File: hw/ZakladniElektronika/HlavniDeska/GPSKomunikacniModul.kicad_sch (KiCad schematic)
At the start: 5 parts, among them J3 Conn_2Rows-75Pins

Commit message: Nastin schematu
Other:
- moved on the sheet: D125, J3, R5, R8, U53

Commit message: Zavazbení zapínání
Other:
- note added: "W_DISABLE"
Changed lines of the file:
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@@
     (stroke (width 0.25) (type default) (color 0 0 0 1))
+  )
+  (text "W_DISABLE" (at 149.86 118.11 0)
+    (effects (font (size 1.27 1.27)) (justify left bottom))
   )
   (label "SIM_CD" (at 151.13 157.48 0) (fields_autoplaced)
@@
         )
         (path "/99cd3e15-4eb6-4cbb-8726-789aedd3df15/c3b70d9b-0dcb-4344-9507-13ff5b4c000e/2d5c8383-b4dd-4e50-a76e-5d9de1ae531a"
-          (reference "LED") (unit 1)
-        )
-      )
+          (reference "LED6") (unit 1)
+        )
+      )

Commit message: USB_multiplexer a přehlednost
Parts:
- added R13: 200k, Resistor_SMD:R_0402_1005Metric, symbol Device:R
- added R14, R16: 0-nc, symbol Device:R
- added R15, R17: 0, Resistor_SMD:R_0805_2012Metric_Pad1.20x1.40mm_HandSolder, symbol Device:R
- added U5: PCA9306DC, Package_SO:VSSOP-8_2.3x2mm_P0.5mm, symbol Interface:PCA9306DC
- added U6, U8: TXB0304RUT, Package_DFN_QFN:Texas_R-PUQFN-N12, symbol Logic_LevelTranslator:TXB0304RUT
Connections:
- net 1V8: now also U5.2 (VREF1), U6.1 (VCCA), U8.1 (VCCA)
- net 3V3: now also R13.1, U6.11 (VCCB)
- net CTS: now also U6.8 (B3)
- net DTR: now also U8.9 (B2)
- net GND: now also U5.1 (GND), U6.6 (GND), U8.6 (GND)
- net RST: now also U8.10 (B1)
- net RTS: now also U6.7 (B4)
- net RXD: now also U6.9 (B2)
- net SCL: now also U5.6 (SCL2)
- net SCL(1.8V): now also U5.3 (SCL1)
- net SDA: now also U5.5 (SDA2)
- net SDA(1.8V): now also U5.4 (SDA1)
- net TXD: now also U6.10 (B1)
- net UART_CTS(O)(1.8V): now also U6.4 (A3)
- net UART_DTR(I)(1.8V): now also U8.3 (A2)
- net UART_RTS(I)(1.8V): now also U6.5 (A4)
- net UART_RXD(I)(1.8V): now also R14.1, R15.1, U6.3 (A2); no longer J3.58 (Pin_58)
- net UART_TXD(O)(1.8V): now also R16.1, R17.1, U6.2 (A1); no longer J3.60 (Pin_60)
- net at J3.62 (Pin_62): now also R15.2
- net at J3.64 (Pin_64): now also R17.2
- net PNU0/LVD: no longer names the net of J3.67 (Pin_67)
- net PNU0/LVD: now also U8.2 (A1)
- net USB_D+ renamed D-
- net USB_D- renamed D+
- net WoWWAN(INT) renamed INT
- new net: R13.2, U5.7 (VREF2), U5.8 (EN)
- new net: J3.60 (Pin_60), R16.2
- new net: J3.58 (Pin_58), R14.2
- no-connect marks 37 -> 35
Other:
- removed sheet PNU0
- removed sheet PNU1
- removed sheet PNU2
- removed sheet PNU3
- removed sheet PNU4
- removed sheet PNU5
- removed sheet PNU6
- removed sheet PNU7
- moved on the sheet: D125, R5, U53

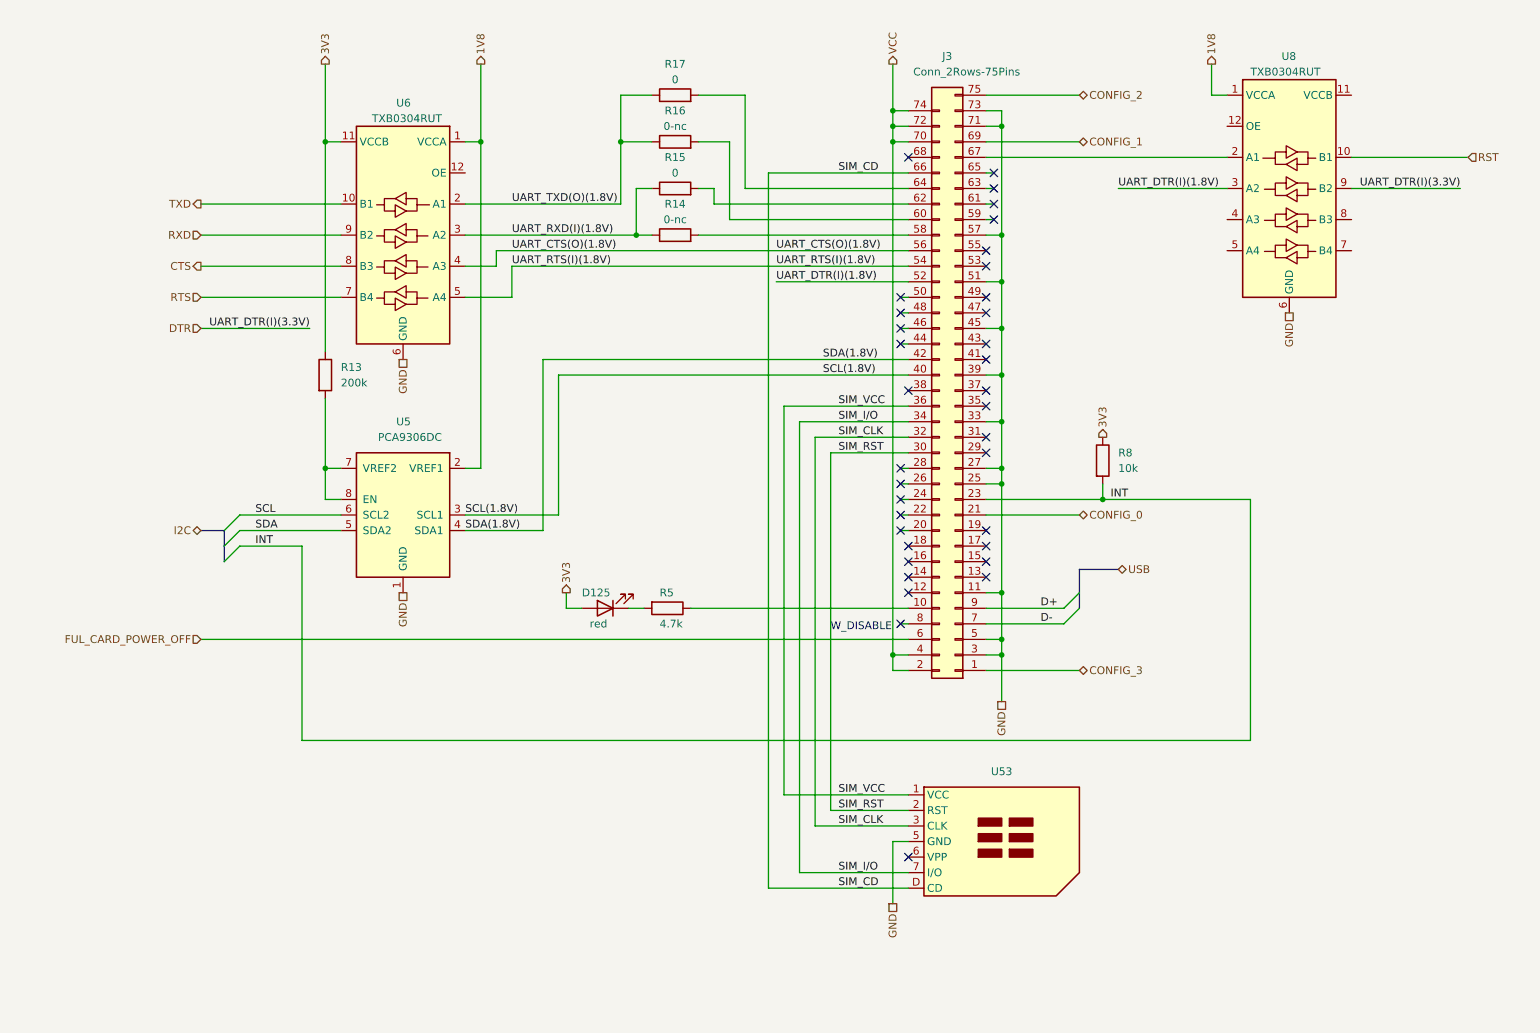
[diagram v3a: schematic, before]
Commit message: Likvidace MiniUI jako samostatné desky a výběr všech komponent
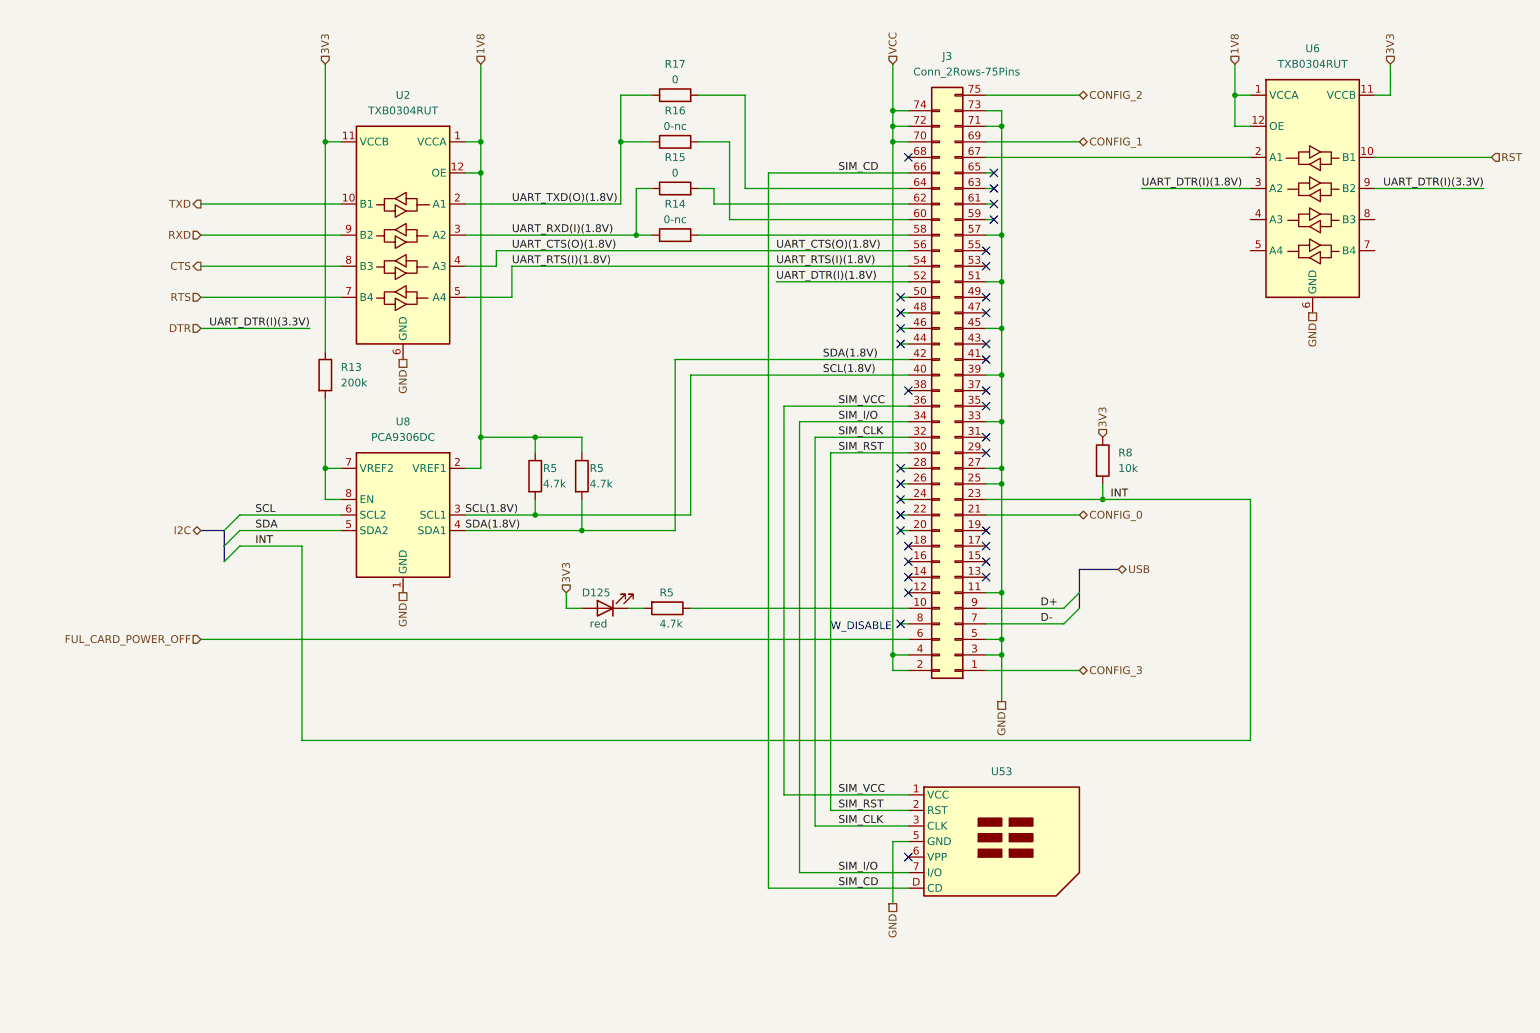
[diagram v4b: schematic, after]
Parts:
- removed U5: PCA9306DC, Package_SO:VSSOP-8_2.3x2mm_P0.5mm, symbol Interface:PCA9306DC
- removed U6, U8: TXB0304RUT, Package_DFN_QFN:Texas_R-PUQFN-N12, symbol Logic_LevelTranslator:TXB0304RUT
- added R5 (x2): 4.7k, Resistor_SMD:R_0402_1005Metric, symbol Device:R
- added U2, U6: TXB0304RUT, Package_DFN_QFN:Texas_R-PUQFN-N12, symbol RKL-BusCnverters:TXB0304RUT
- added U8: PCA9306DC, Package_SO:VSSOP-8_2.3x2mm_P0.5mm, symbol RKL-BusCnverters:PCA9306DC
- J3: footprint Robotarna_KiCad_Library:Conn_M2 -> RKL-Connectors:Conn_M2; Basic/Extended (none) -> E
- R14, R16: footprint (none) -> Resistor_SMD:R_0805_2012Metric_Pad1.20x1.40mm_HandSolder; JLCPCB_IGNORE (none) -> ignore
- R15, R17: Basic/Extended (none) -> B; LCSC C908865 -> C17477
- R5: footprint Resistor_SMD:R_0201_0603Metric -> Resistor_SMD:R_0402_1005Metric; Basic/Extended E -> B; LCSC C270346 -> C25900
- R8: Basic/Extended (none) -> B
- U53: footprint (none) -> RKL-Connectors:SMN-305-ARP7; Basic/Extended (none) -> E; LCSC (none) -> C720512
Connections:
- net 1V8: now also R5.1, R5.1, U2.1 (VCCA), U2.12 (OE), U6.1 (VCCA), U6.12 (OE), U8.2 (VREF1)
- net 3V3: now also U2.11 (VCCB), U6.11 (VCCB)
- net CTS: now also U2.8 (B3)
- net DTR: now also U6.9 (B2)
- net GND: now also U2.6 (GND), U6.6 (GND), U8.1 (GND)
- net RST: now also U6.10 (B1)
- net RTS: now also U2.7 (B4)
- net RXD: now also U2.9 (B2)
- net SCL: now also U8.6 (SCL2)
- net SCL(1.8V): now also R5.2, U8.3 (SCL1)
- net SDA: now also U8.5 (SDA2)
- net SDA(1.8V): now also R5.2, U8.4 (SDA1)
- net TXD: now also U2.10 (B1)
- net UART_CTS(O)(1.8V): now also U2.4 (A3)
- net UART_DTR(I)(1.8V): now also U6.3 (A2)
- net UART_RTS(I)(1.8V): now also U2.5 (A4)
- net UART_RXD(I)(1.8V): now also U2.3 (A2)
- net UART_TXD(O)(1.8V): now also U2.2 (A1)
- net at R13.2: now also U8.7 (VREF2), U8.8 (EN)
- net at J3.67 (Pin_67): now also U6.2 (A1)

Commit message: Výmněna ochrany baterie
Předchozí ochranný čip JLCPCB nemělo na skladě
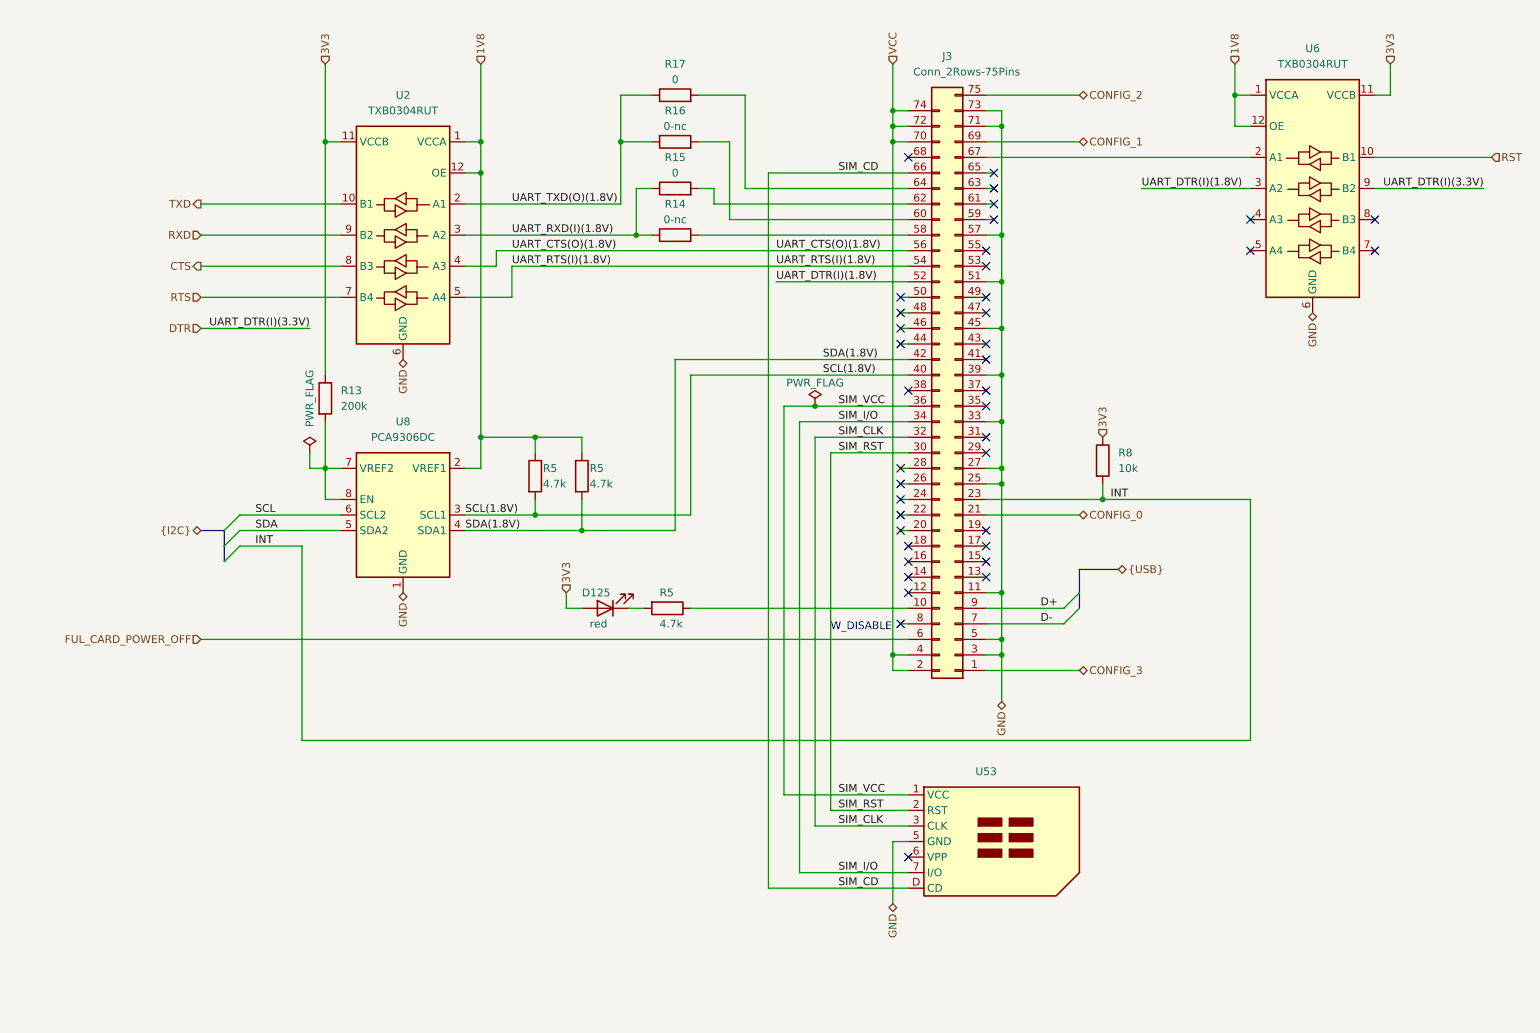
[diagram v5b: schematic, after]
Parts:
- U53: symbol Robotarna_KiCad_Library:SIM -> RKL-Uncategorized:SIM
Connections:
- no-connect marks 35 -> 39
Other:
- moved on the sheet: R13
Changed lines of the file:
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@@
   (junction (at 92.71 38.1) (diameter 0) (color 0 0 0 0)
+  )
+  (junction (at 147.32 81.28) (diameter 0) (color 0 0 0 0)
   )
   (junction (at 67.31 38.1) (diameter 0) (color 0 0 0 0)
@@
   (no_connect (at 161.29 66.04))
   (no_connect (at 162.56 106.68))
+  (no_connect (at 238.76 50.8))
   (no_connect (at 161.29 96.52))
   (no_connect (at 175.26 63.5))
@@
   (no_connect (at 175.26 55.88))
   (no_connect (at 161.29 71.12))
+  (no_connect (at 218.44 55.88))
   (no_connect (at 176.53 43.18))
   (no_connect (at 162.56 78.74))
+  (no_connect (at 238.76 55.88))
   (no_connect (at 175.26 78.74))
+  (no_connect (at 218.44 50.8))
   (no_connect (at 162.56 40.64))
   (no_connect (at 161.29 63.5))
@@
     (stroke (width 0) (type default))
   )
+  (wire (pts (xy 147.32 81.28) (xy 162.56 81.28))
+    (stroke (width 0) (type default))
+  )
   (wire (pts (xy 162.56 76.2) (xy 127 76.2))
     (stroke (width 0) (type default))
@@
   )
   (wire (pts (xy 162.56 93.98) (xy 161.29 93.98))
+    (stroke (width 0) (type default))
+  )
+  (wire (pts (xy 147.32 81.28) (xy 142.24 81.28))
     (stroke (width 0) (type default))
   )
@@
     (stroke (width 0) (type default))
   )
-  (wire (pts (xy 67.31 80.01) (xy 67.31 91.44))
+  (wire (pts (xy 67.31 83.82) (xy 67.31 91.44))
     (stroke (width 0) (type default))
   )
@@
     (stroke (width 0.25) (type default) (color 0 0 0 1))
   )
+  (wire (pts (xy 64.77 91.44) (xy 64.77 88.9))
+    (stroke (width 0) (type default))
+  )
   (wire (pts (xy 160.02 35.56) (xy 160.02 38.1))
     (stroke (width 0) (type default) (color 255 26 33 1))
@@
     (stroke (width 0) (type default))
   )
-  (wire (pts (xy 162.56 81.28) (xy 142.24 81.28))
-    (stroke (width 0) (type default))
-  )
   (wire (pts (xy 95.25 55.88) (xy 162.56 55.88))
     (stroke (width 0) (type default))
@@
     (stroke (width 0) (type default))
   )
-  (wire (pts (xy 67.31 38.1) (xy 67.31 72.39))
+  (wire (pts (xy 67.31 38.1) (xy 67.31 76.2))
     (stroke (width 0) (type default))
   )
   (wire (pts (xy 162.56 149.86) (xy 147.32 149.86))
+    (stroke (width 0) (type default))
+  )
+  (wire (pts (xy 64.77 91.44) (xy 67.31 91.44))
     (stroke (width 0) (type default))
   )
@@
     (effects (font (size 1.27 1.27)) (justify left))
   )
-  (hierarchical_label "GND" (shape passive) (at 80.01 73.66 270) (fields_autoplaced)
+  (hierarchical_label "GND" (shape bidirectional) (at 80.01 73.66 270) (fields_autoplaced)
     (effects (font (size 1.27 1.27)) (justify right))
   )
-  (hierarchical_label "USB" (shape bidirectional) (at 196.85 107.95 0) (fields_autoplaced)
+  (hierarchical_label "{USB}" (shape bidirectional) (at 196.85 107.95 0) (fields_autoplaced)
     (effects (font (size 1.27 1.27)) (justify left))
   )
@@
     (effects (font (size 1.27 1.27)) (justify left))
   )
+  (hierarchical_label "{I2C}" (shape bidirectional) (at 46.99 101.6 180) (fields_autoplaced)
+    (effects (font (size 1.27 1.27)) (justify right))
+  )
   (hierarchical_label "DTR" (shape input) (at 46.99 68.58 180) (fields_autoplaced)
     (effects (font (size 1.27 1.27)) (justify right))
@@
     (effects (font (size 1.27 1.27)) (justify right))
   )
-  (hierarchical_label "GND" (shape passive) (at 177.8 129.54 270) (fields_autoplaced)
+  (hierarchical_label "GND" (shape bidirectional) (at 177.8 129.54 270) (fields_autoplaced)
     (effects (font (size 1.27 1.27)) (justify right))
   )
-  (hierarchical_label "GND" (shape passive) (at 80.01 111.76 270) (fields_autoplaced)
+  (hierarchical_label "GND" (shape bidirectional) (at 80.01 111.76 270) (fields_autoplaced)
     (effects (font (size 1.27 1.27)) (justify right))
   )
@@
     (effects (font (size 1.27 1.27)) (justify left))
   )
-  (hierarchical_label "I2C" (shape bidirectional) (at 46.99 101.6 180) (fields_autoplaced)
-    (effects (font (size 1.27 1.27)) (justify right))
-  )
-  (hierarchical_label "GND" (shape passive) (at 160.02 162.56 270) (fields_autoplaced)
+  (hierarchical_label "GND" (shape bidirectional) (at 160.02 162.56 270) (fields_autoplaced)
     (effects (font (size 1.27 1.27)) (justify right))
   )
@@
     (effects (font (size 1.27 1.27)) (justify right))
   )
-  (hierarchical_label "GND" (shape passive) (at 228.6 66.04 270) (fields_autoplaced)
+  (hierarchical_label "GND" (shape bidirectional) (at 228.6 66.04 270) (fields_autoplaced)
     (effects (font (size 1.27 1.27)) (justify right))
   )
@@
     )
   )
-  (symbol (lib_id "Device:R") (at 67.31 76.2 0) (unit 1)
-    (in_bom yes) (on_board yes) (dnp no)
-    (property "Reference" "R13" (at 69.85 74.93 0)
+  (symbol (lib_id "Device:R") (at 67.31 80.01 0) (unit 1)
+    (in_bom yes) (on_board yes) (dnp no)
+    (property "Reference" "R13" (at 69.85 78.74 0)
       (effects (font (size 1.27 1.27)) (justify left))
     )
-    (property "Value" "200k" (at 69.85 77.47 0)
+    (property "Value" "200k" (at 69.85 81.28 0)
       (effects (font (size 1.27 1.27)) (justify left))
     )
-    (property "Footprint" "Resistor_SMD:R_0402_1005Metric" (at 65.532 76.2 90)
-      (effects (font (size 1.27 1.27)) hide)
-    )
-    (property "Datasheet" "~" (at 67.31 76.2 0)
-      (effects (font (size 1.27 1.27)) hide)
-    )
-    (property "LCSC" "C25764" (at 67.31 76.2 0)
-      (effects (font (size 1.27 1.27)) hide)
-    )
-    (property "Basic/Extended" "B" (at 67.31 76.2 0)
+    (property "Footprint" "Resistor_SMD:R_0402_1005Metric" (at 65.532 80.01 90)
+      (effects (font (size 1.27 1.27)) hide)
+    )
+    (property "Datasheet" "~" (at 67.31 80.01 0)
+      (effects (font (size 1.27 1.27)) hide)
+    )
+    (property "LCSC" "C25764" (at 67.31 80.01 0)
+      (effects (font (size 1.27 1.27)) hide)
+    )
+    (property "Basic/Extended" "B" (at 67.31 80.01 0)
       (effects (font (size 1.27 1.27)) hide)
     )
@@
     )
   )
-  (symbol (lib_id "Robotarna_KiCad_Library:SIM") (at 175.26 143.51 0) (unit 1)
-    (in_bom yes) (on_board yes) (dnp no) (fields_autoplaced)
-    (property "Reference" "U53" (at 177.8 140.97 0)
+  (symbol (lib_id "RKL-Uncategorized:SIM") (at 175.26 143.51 0) (unit 1)
+    (in_bom yes) (on_board yes) (dnp no)
+    (property "Reference" "U53" (at 175.26 140.97 0)
       (effects (font (size 1.27 1.27)))
     )
@@
         (path "/99cd3e15-4eb6-4cbb-8726-789aedd3df15/c3b70d9b-0dcb-4344-9507-13ff5b4c000e/2d5c8383-b4dd-4e50-a76e-5d9de1ae531a"
           (reference "U53") (unit 1)
+        )
+      )
+    )
+  )
+  (symbol (lib_id "power:PWR_FLAG") (at 64.77 88.9 0) (unit 1)
+    (in_bom yes) (on_board yes) (dnp no)
+    (property "Reference" "#FLG05" (at 64.77 86.995 0)
+      (effects (font (size 1.27 1.27)) hide)
+    )
+    (property "Value" "PWR_FLAG" (at 64.77 80.01 90)
+      (effects (font (size 1.27 1.27)))
+    )
+    (property "Footprint" "" (at 64.77 88.9 0)
+      (effects (font (size 1.27 1.27)) hide)
+    )
+    (property "Datasheet" "~" (at 64.77 88.9 0)
+      (effects (font (size 1.27 1.27)) hide)
+    )
+    (pin "1")
+    (instances
+      (project "ZakladniElektronika"
+        (path "/99cd3e15-4eb6-4cbb-8726-789aedd3df15"
+          (reference "#FLG05") (unit 1)
+        )
+        (path "/99cd3e15-4eb6-4cbb-8726-789aedd3df15/c3b70d9b-0dcb-4344-9507-13ff5b4c000e/2d5c8383-b4dd-4e50-a76e-5d9de1ae531a"
+          (reference "#FLG08") (unit 1)
         )
       )
@@
         )
       )
+    )
+  )
+  (symbol (lib_id "power:PWR_FLAG") (at 147.32 81.28 0) (unit 1)
+    (in_bom yes) (on_board yes) (dnp no)
+    (property "Reference" "#FLG05" (at 147.32 79.375 0)
+      (effects (font (size 1.27 1.27)) hide)
+    )
+    (property "Value" "PWR_FLAG" (at 147.32 77.47 0)
+      (effects (font (size 1.27 1.27)))
+    )
+    (property "Footprint" "" (at 147.32 81.28 0)
+      (effects (font (size 1.27 1.27)) hide)
+    )
+    (property "Datasheet" "~" (at 147.32 81.28 0)
+      (effects (font (size 1.27 1.27)) hide)
+    )
+    (pin "1")
+    (instances
+      (project "ZakladniElektronika"
+        (path "/99cd3e15-4eb6-4cbb-8726-789aedd3df15"
+          (reference "#FLG05") (unit 1)
+        )
+        (path "/99cd3e15-4eb6-4cbb-8726-789aedd3df15/c3b70d9b-0dcb-4344-9507-13ff5b4c000e/2d5c8383-b4dd-4e50-a76e-5d9de1ae531a"
+          (reference "#FLG07") (unit 1)
+        )
+      )
